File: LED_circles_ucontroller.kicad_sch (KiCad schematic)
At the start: 20 parts, among them J1 Conn_ARM_SWD_EDGE, U75 M95256-WMN6P, U76 M95256-WMN6P, U77 STM32G071KBTxN

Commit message: More layout
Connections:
- net +3.3V: now also U77.4 (VDD)
- net HOLD: now also U77.21 (PA10/UCPD1_DBCC2); no longer U77.2 (PC14)
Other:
- moved on the sheet: TP1, TP2
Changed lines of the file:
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@@
+	(wire
+		(pts
+			(xy 283.21 58.42) (xy 283.21 64.77)
+		)
+		(stroke
+			(width 0)
+			(type default)
+		)
+	)
 	(wire
 		(pts
@@
 	(wire
 		(pts
-			(xy 238.76 92.71) (xy 257.81 92.71)
+			(xy 327.66 102.87) (xy 308.61 102.87)
 		)
 		(stroke
@@
 	)
 	(label "HOLD"
-		(at 238.76 92.71 0)
+		(at 327.66 102.87 180)
 		(effects
 			(font
 				(size 1.27 1.27)
 			)
-			(justify left bottom)
+			(justify right bottom)
 		)
 	)
@@
 	(symbol
 		(lib_id "Connector:TestPoint")
-		(at 415.29 76.2 0)
+		(at 379.73 102.87 0)
 		(unit 1)
 		(exclude_from_sim no)
@@
 		(fields_autoplaced yes)
 		(property "Reference" "TP2"
-			(at 417.83 71.6279 0)
+			(at 382.27 98.2979 0)
 			(effects
 				(font
@@
 		)
 		(property "Value" "TestPoint"
-			(at 417.83 74.1679 0)
+			(at 382.27 100.8379 0)
 			(effects
 				(font
@@
 		)
 		(property "Footprint" "TestPoint:TestPoint_Pad_3.0x3.0mm"
-			(at 420.37 76.2 0)
+			(at 384.81 102.87 0)
 			(effects
 				(font
@@
 		)
 		(property "Datasheet" "~"
-			(at 420.37 76.2 0)
+			(at 384.81 102.87 0)
 			(effects
 				(font
@@
 		)
 		(property "Description" "test point"
-			(at 415.29 76.2 0)
+			(at 379.73 102.87 0)
 			(effects
 				(font
@@
 	(symbol
 		(lib_id "Connector:TestPoint")
-		(at 400.05 77.47 0)
+		(at 364.49 104.14 0)
 		(unit 1)
 		(exclude_from_sim no)
@@
 		(fields_autoplaced yes)
 		(property "Reference" "TP1"
-			(at 402.59 72.8979 0)
+			(at 367.03 99.5679 0)
 			(effects
 				(font
@@
 		)
 		(property "Value" "TestPoint"
-			(at 402.59 75.4379 0)
+			(at 367.03 102.1079 0)
 			(effects
 				(font
@@
 		)
 		(property "Footprint" "TestPoint:TestPoint_Pad_3.0x3.0mm"
-			(at 405.13 77.47 0)
+			(at 369.57 104.14 0)
 			(effects
 				(font
@@
 		)
 		(property "Datasheet" "~"
-			(at 405.13 77.47 0)
+			(at 369.57 104.14 0)
 			(effects
 				(font
@@
 		)
 		(property "Description" "test point"
-			(at 400.05 77.47 0)
+			(at 364.49 104.14 0)
 			(effects
 				(font
@@
 					(unit 1)
 				)
+			)
+		)
+	)
+	(symbol
+		(lib_id "power:+3.3V")
+		(at 283.21 58.42 0)
+		(unit 1)
+		(exclude_from_sim no)
+		(in_bom yes)
+		(on_board yes)
+		(dnp no)
+		(fields_autoplaced yes)
+		(property "Reference" "#PWR0157"
+			(at 283.21 62.23 0)
+			(effects
+				(font
+					(size 1.27 1.27)
+				)
+				(hide yes)
+			)
+		)
+		(property "Value" "+3.3V"
+			(at 283.21 53.34 0)
+			(effects
+				(font
+					(size 1.27 1.27)
+				)
+			)
+		)
+		(property "Footprint" ""
+			(at 283.21 58.42 0)
+			(effects
+				(font
+					(size 1.27 1.27)
+				)
+				(hide yes)
+			)
+		)
+		(property "Datasheet" ""
+			(at 283.21 58.42 0)
+			(effects
+				(font
+					(size 1.27 1.27)
+				)
+				(hide yes)
+			)
+		)
+		(property "Description" "Power symbol creates a global label with name \"+3.3V\""
+			(at 283.21 58.42 0)
+			(effects
+				(font
+					(size 1.27 1.27)
+				)
+				(hide yes)
+			)
+		)
+		(pin "1"
+		)
+		(instances
+			(project "LED_circles"
+				(path "/fee5cc62-df5b-4e25-a1c9-d9673ac3b8e2/a02ddc3d-cba5-487a-854d-aeab8652491a"
+					(reference "#PWR0157")
+					(unit 1)
+				)

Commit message: More layout
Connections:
- net RX: now also TP2.1
- net TX: now also TP1.1
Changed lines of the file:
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@@
+	(wire
+		(pts
+			(xy 349.25 95.25) (xy 349.25 109.22)
+		)
+		(stroke
+			(width 0)
+			(type default)
+		)
+	)
 	(wire
 		(pts
@@
 	(wire
 		(pts
-			(xy 320.04 95.25) (xy 308.61 95.25)
+			(xy 308.61 95.25) (xy 349.25 95.25)
+		)
+		(stroke
+			(width 0)
+			(type default)
+		)
+	)
+	(wire
+		(pts
+			(xy 379.73 113.03) (xy 379.73 102.87)
 		)
 		(stroke
@@
 	(wire
 		(pts
-			(xy 320.04 100.33) (xy 308.61 100.33)
+			(xy 308.61 100.33) (xy 346.71 100.33)
 		)
 		(stroke
@@
 	(wire
 		(pts
+			(xy 346.71 100.33) (xy 346.71 113.03)
+		)
+		(stroke
+			(width 0)
+			(type default)
+		)
+	)
+	(wire
+		(pts
 			(xy 186.69 34.29) (xy 186.69 36.83)
 		)
@@
 	(wire
 		(pts
+			(xy 346.71 113.03) (xy 379.73 113.03)
+		)
+		(stroke
+			(width 0)
+			(type default)
+		)
+	)
+	(wire
+		(pts
 			(xy 308.61 87.63) (xy 322.58 87.63)
 		)
@@
 	(wire
 		(pts
+			(xy 349.25 109.22) (xy 364.49 109.22)
+		)
+		(stroke
+			(width 0)
+			(type default)
+		)
+	)
+	(wire
+		(pts
 			(xy 276.86 21.59) (xy 276.86 24.13)
 		)
@@
 		)
 		(stroke
+			(width 0)
+			(type default)
+		)
+	)
+	(wire
+		(pts
+			(xy 364.49 109.22) (xy 364.49 104.14)
+		)
+		(stroke

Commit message: More layout
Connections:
- net EEPROM1_CS: now also U77.31 (PB7); no longer U77.1 (PB9)
- net EEPROM2_CS: now also U77.30 (PB6); no longer U77.17 (PB15)
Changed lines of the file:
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@@
 	(wire
 		(pts
-			(xy 238.76 113.03) (xy 257.81 113.03)
+			(xy 238.76 107.95) (xy 257.81 107.95)
 		)
 		(stroke
@@
 	(wire
 		(pts
-			(xy 238.76 115.57) (xy 257.81 115.57)
+			(xy 238.76 105.41) (xy 257.81 105.41)
 		)
 		(stroke
@@
 	)
 	(label "EEPROM1_CS"
-		(at 238.76 113.03 0)
+		(at 238.76 107.95 0)
 		(effects
 			(font
@@
 	)
 	(label "EEPROM2_CS"
-		(at 238.76 115.57 0)
-		(effects
-			(font
+		(at 238.76 105.41 0)
+		(effects
+			(font

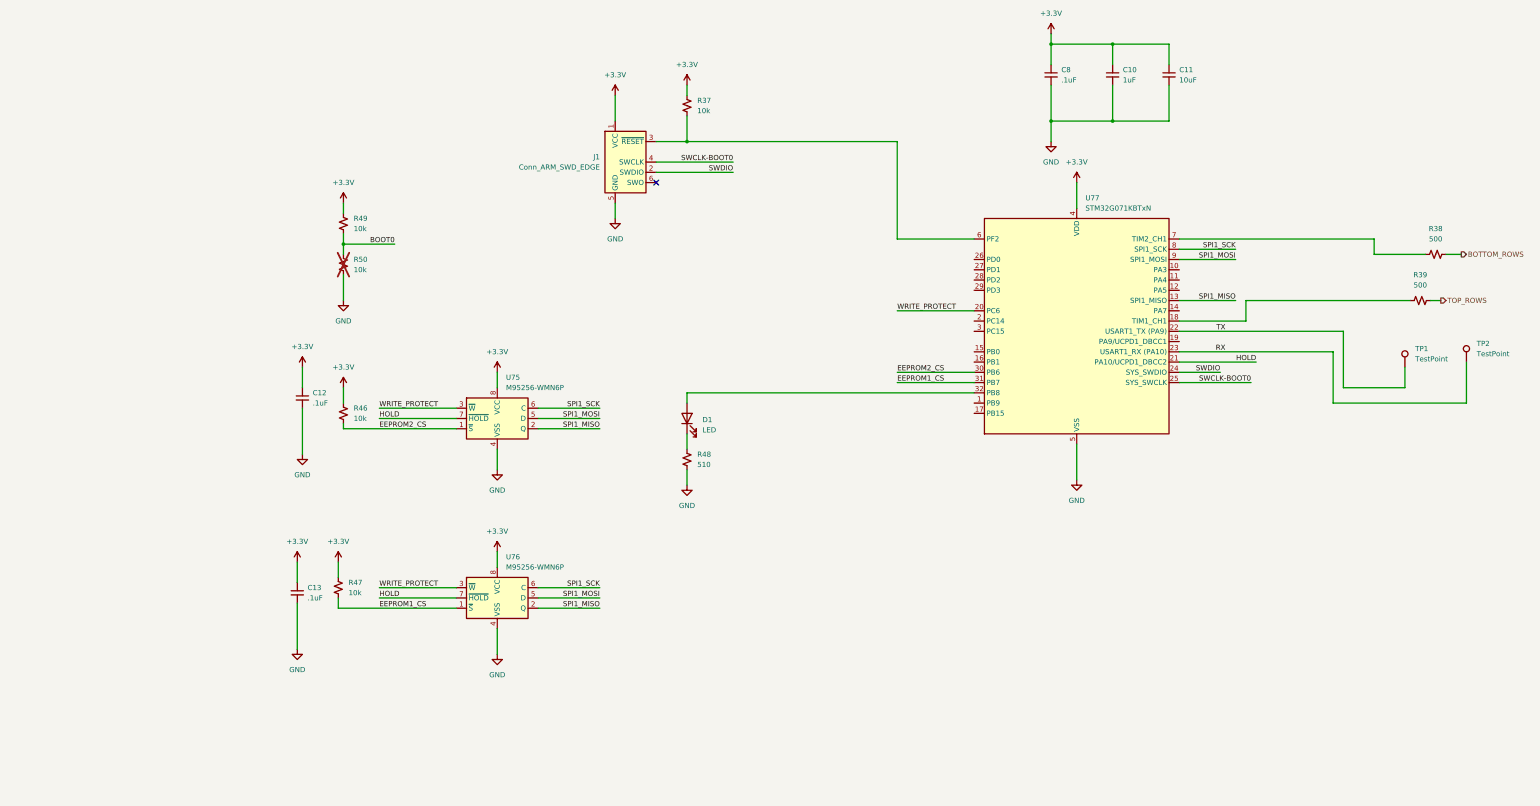
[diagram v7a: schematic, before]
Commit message: Pin swapping on pogo pins
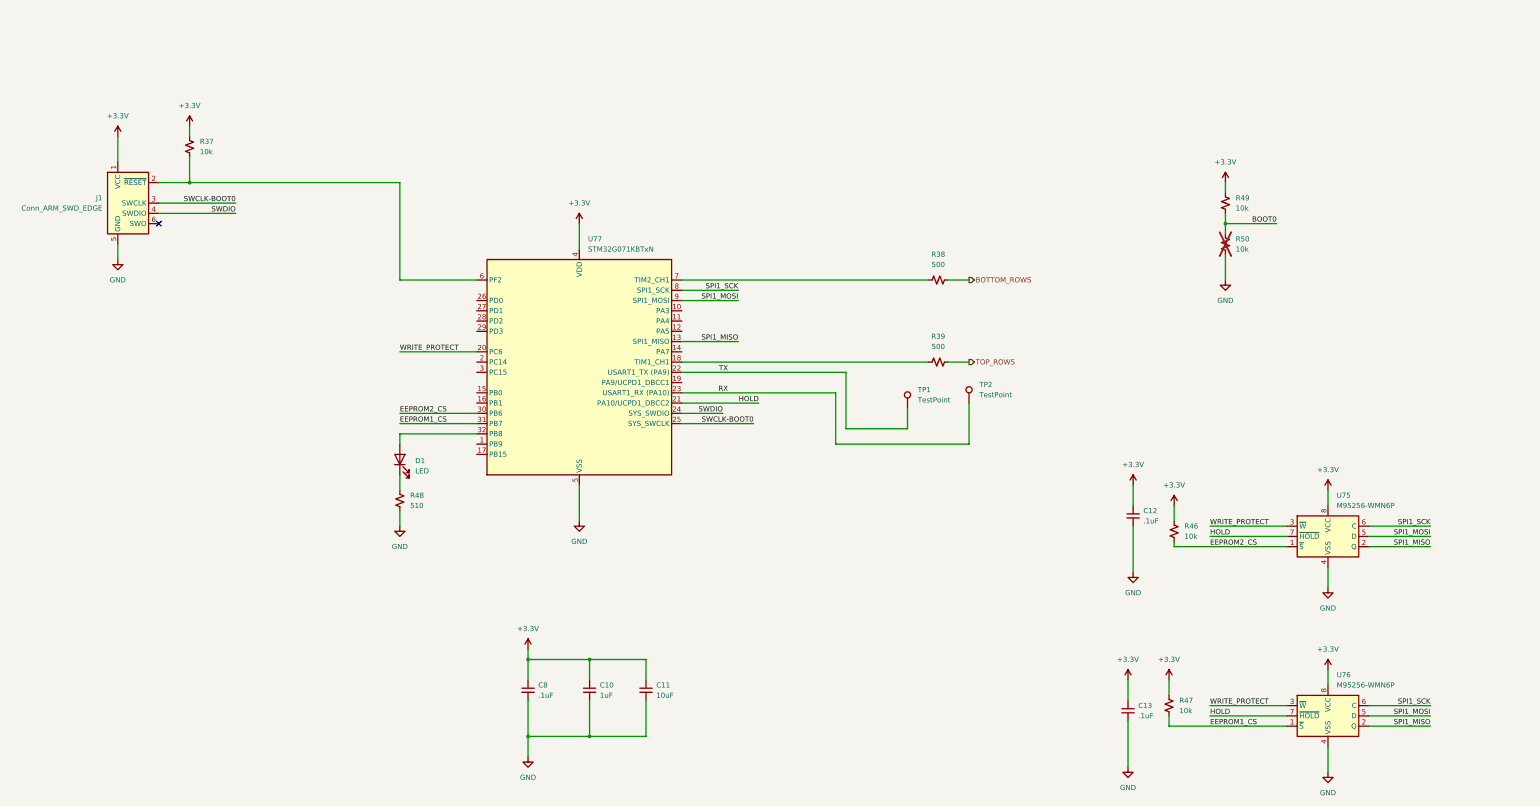
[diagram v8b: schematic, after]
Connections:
- net SWCLK-BOOT0: now also J1.3 (SWCLK); no longer J1.4 (SWCLK)
- net SWDIO: now also J1.4 (SWDIO); no longer J1.2 (SWDIO)
- net at R37.2, U77.6 (PF2): now also J1.2 (~{RESET}); no longer J1.3 (~{RESET})
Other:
- moved on the sheet: C10, C11, C12, C13, C8, D1, J1, R37, R38, R39, R46, R47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
